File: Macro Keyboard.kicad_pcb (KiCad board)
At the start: 2 copper layers, 101.6 x 123.4 mm, 136 parts, among them J2901 FPC 1x24, Q2901 Q_PJFET_GDS, SW1001 KH-PS1611-54, SW1101 KH-PS1611-54, SW1201 KH-PS1611-54, SW1301 KH-PS1611-54, SW1401 KH-PS1611-54, SW1501 KH-PS1611-54, SW2801 SWITCH TACTILE SPST-NO 50MA 1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, SW601 KH-PS1611-54, SW701 KH-PS1611-54, SW801 KH-PS1611-54, SW901 KH-PS1611-54, U2701 PCA9745BTWJ, U2801 Pico-JER, U301 VEML7700, U401 PI4ULS5V201TAEX

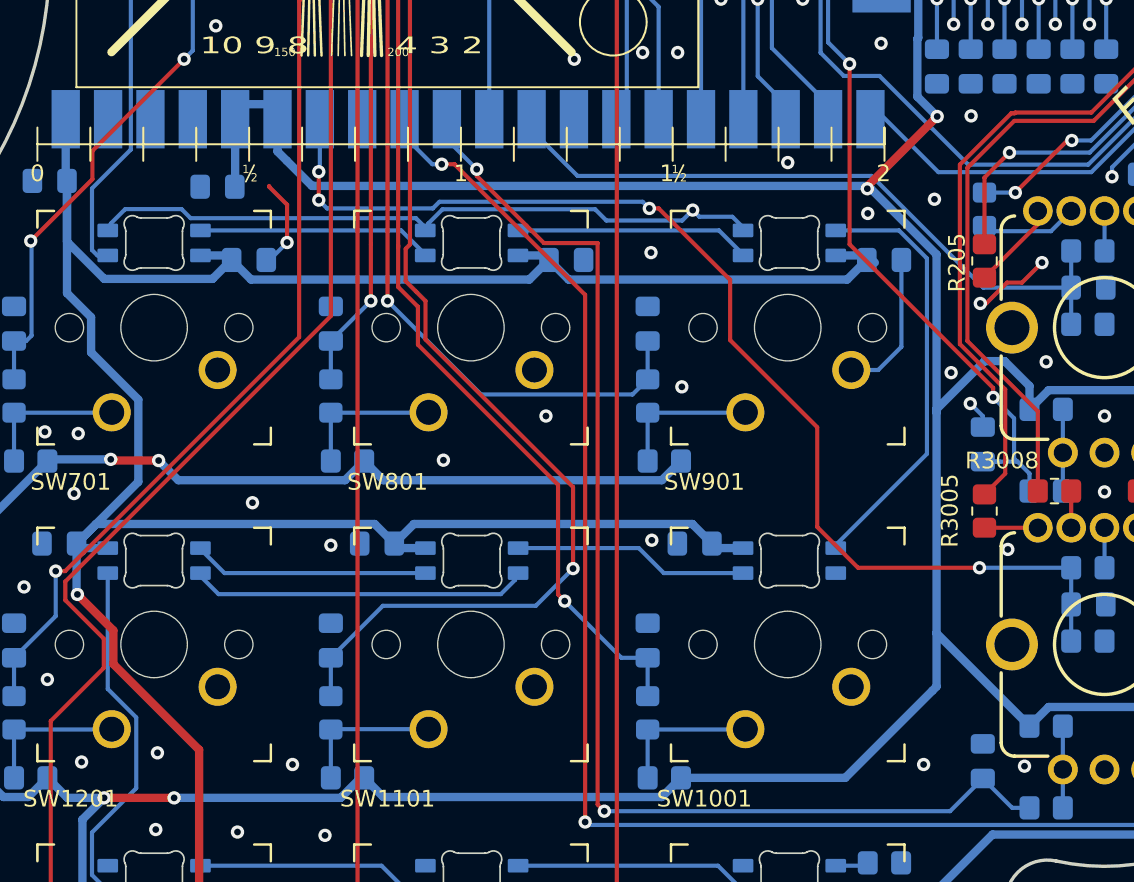
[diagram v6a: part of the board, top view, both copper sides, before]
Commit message: Updated several part orientations to eliminate minimuim clearance issues.
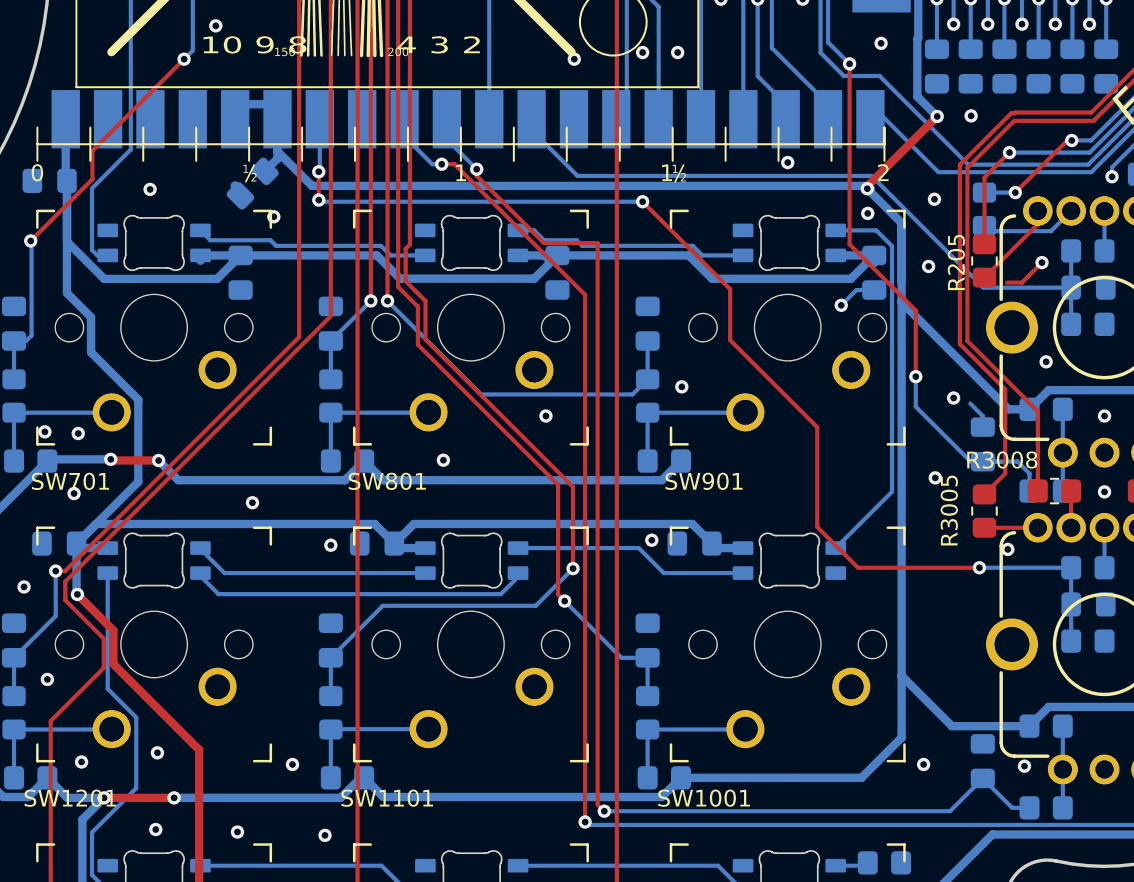
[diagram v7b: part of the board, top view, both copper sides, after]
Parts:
- moved C2801 2.12 mm to (65.9, 81.4), turned to 225 degrees
- moved C2001 0.97 mm to (103.2, 86.7), turned to 90 degrees
- moved C1901 0.93 mm to (84.2, 86.7), turned to 90 degrees
- moved C1801 0.92 mm to (65.2, 86.7), turned to 90 degrees
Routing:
- net GND: track 195.1 -> 139.8 mm
- net /LED 10/Neo LED 05/D_IN: track 26.1 -> 23.3 mm
- net +5V: track 358.7 -> 360.3 mm
- net +3V3: track 463.4 -> 462.3 mm
- net /Pico/GPIO_28_ADC2: track 70.4 -> 69.7 mm

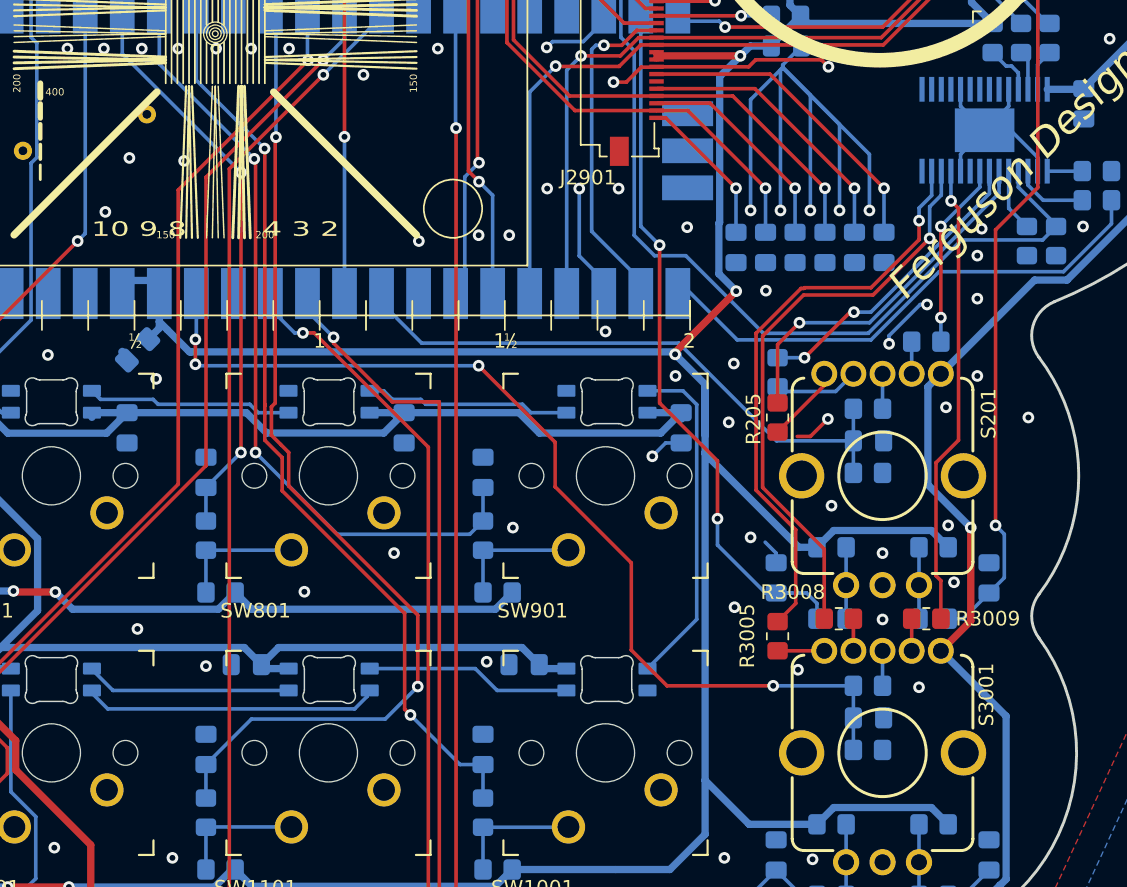
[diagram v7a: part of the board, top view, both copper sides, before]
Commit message: Updated routing to eliminate minimuim clearance issues.
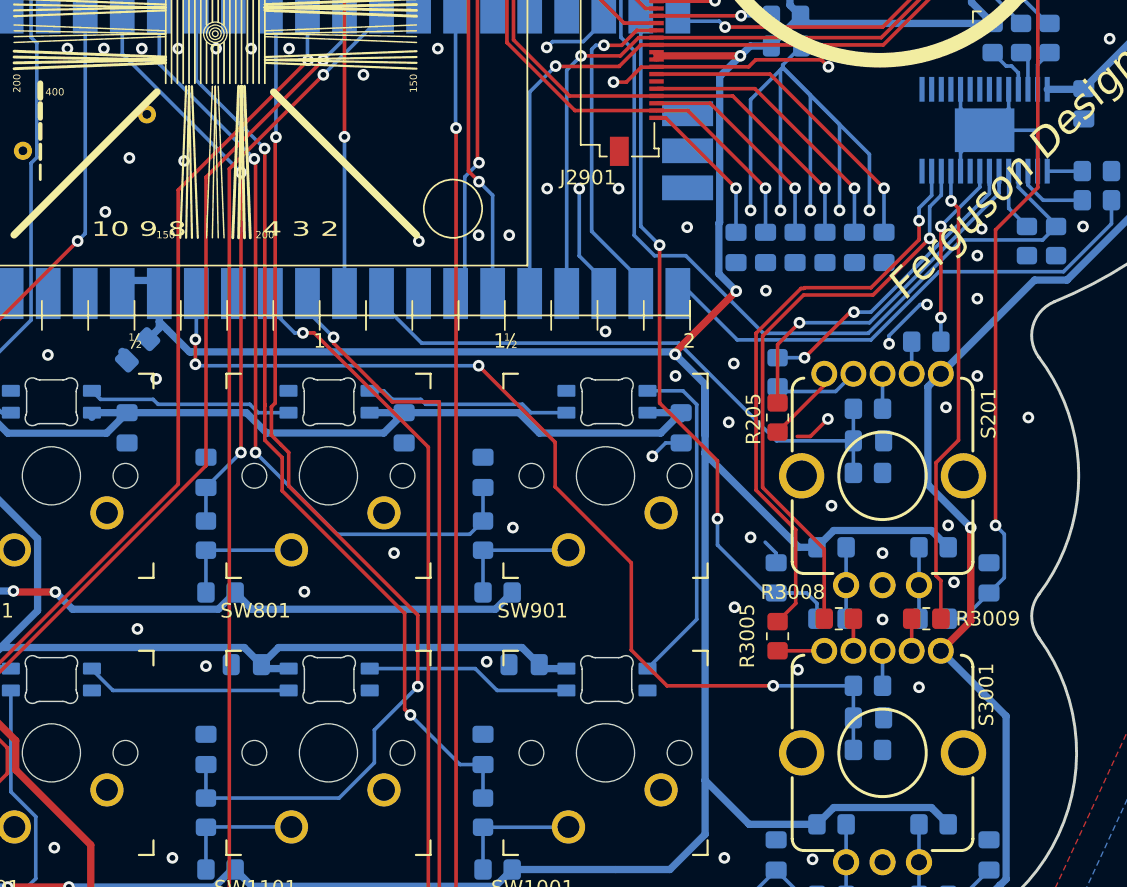
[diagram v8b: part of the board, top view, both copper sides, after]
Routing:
- net GND: track 139.8 -> 122.6 mm
- net /Pico/GPIO_06: track 69.2 -> 71.5 mm
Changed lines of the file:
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@@
     (thickness 1.6)
     (drawings 97)
-    (tracks 1007)
+    (tracks 1008)
     (zones 0)
     (modules 136)
@@
   (via (at 109.9 25.7) (size 0.8) (drill 0.4) (layers F.Cu B.Cu) (net 1))
   (via (at 126.1 25.7) (size 0.8) (drill 0.4) (layers F.Cu B.Cu) (net 1))
-  (segment (start 81.65 105.13) (end 81.65 104.72) (width 0.25) (layer B.Cu) (net 1) (status 20))
-  (segment (start 80.797265 105.982735) (end 81.65 105.13) (width 0.25) (layer B.Cu) (net 1))
-  (segment (start 63.862735 105.982735) (end 80.797265 105.982735) (width 0.25) (layer B.Cu) (net 1))
-  (segment (start 62.6 104.72) (end 63.862735 105.982735) (width 0.25) (layer B.Cu) (net 1) (status 10))
   (via (at 68.7 60.7) (size 0.8) (drill 0.4) (layers F.Cu B.Cu) (net 1))
   (via (at 66.2 60.7) (size 0.8) (drill 0.4) (layers F.Cu B.Cu) (net 1))
@@
   (via (at 114.05 71.8) (size 0.8) (drill 0.4) (layers F.Cu B.Cu) (net 1))
   (via (at 116.1 71.8) (size 0.8) (drill 0.4) (layers F.Cu B.Cu) (net 1))
-  (segment (start 122.349 67.951) (end 124 66.3) (width 0.25) (layer B.Cu) (net 1) (status 20))
-  (segment (start 122.349 69.1067) (end 122.349 67.951) (width 0.25) (layer B.Cu) (net 1) (status 10))
-  (segment (start 125.778802 66.3) (end 124 66.3) (width 0.25) (layer B.Cu) (net 1) (status 30))
-  (segment (start 127.6322 68.153398) (end 125.778802 66.3) (width 0.25) (layer B.Cu) (net 1) (status 20))
-  (segment (start 127.6322 69.1067) (end 127.6322 68.153398) (width 0.25) (layer B.Cu) (net 1) (status 10))
-  (segment (start 122.349 64.649) (end 124 66.3) (width 0.25) (layer B.Cu) (net 1) (status 20))
-  (segment (start 122.349 63.4933) (end 122.349 64.649) (width 0.25) (layer B.Cu) (net 1) (status 10))
-  (segment (start 125.651 64.649) (end 124 66.3) (width 0.25) (layer B.Cu) (net 1) (status 20))
-  (segment (start 125.651 63.4933) (end 125.651 64.649) (width 0.25) (layer B.Cu) (net 1) (status 10))
   (via (at 132.9 49.05) (size 0.8) (drill 0.4) (layers F.Cu B.Cu) (net 1))
   (via (at 129.5 53.45) (size 0.8) (drill 0.4) (layers F.Cu B.Cu) (net 1))
@@
   (segment (start 107.82 61.95) (end 108.3 61.47) (width 0.25) (layer F.Cu) (net 1))
   (segment (start 112.81 61.47) (end 113.29 61.95) (width 0.25) (layer F.Cu) (net 1))
-  (segment (start 108.3 61.47) (end 112.81 61.47) (width 0.25) (layer F.Cu) (net 1))
   (segment (start 109.7 98.0375) (end 110.7375 98.0375) (width 0.25) (layer B.Cu) (net 2) (status 10))
   (segment (start 112.5 98.75) (end 111.775 98.025) (width 0.25) (layer B.Cu) (net 2))
@@
   (via (at 106.45 86.33) (size 0.8) (drill 0.4) (layers F.Cu B.Cu) (net 1))
   (via (at 106.85 99.01) (size 0.8) (drill 0.4) (layers F.Cu B.Cu) (net 1))
+  (segment (start 108.3 61.47) (end 112.81 61.47) (width 0.25) (layer F.Cu) (net 1))
+  (segment (start 125.778802 66.3) (end 124 66.3) (width 0.25) (layer B.Cu) (net 1))
+  (segment (start 127.6322 69.1067) (end 127.6322 66.3122) (width 0.25) (layer B.Cu) (net 1))
+  (segment (start 127.62 66.3) (end 124 66.3) (width 0.25) (layer B.Cu) (net 1))
+  (segment (start 127.6322 66.3122) (end 127.62 66.3) (width 0.25) (layer B.Cu) (net 1))
+  (segment (start 122.349 69.1067) (end 122.349 67.831) (width 0.25) (layer B.Cu) (net 1))
+  (segment (start 123.88 66.3) (end 124 66.3) (width 0.25) (layer B.Cu) (net 1))
+  (segment (start 122.349 67.831) (end 123.88 66.3) (width 0.25) (layer B.Cu) (net 1))
+  (segment (start 122.349 63.4933) (end 122.349 64.799) (width 0.25) (layer B.Cu) (net 1))
+  (segment (start 123.85 66.3) (end 124 66.3) (width 0.25) (layer B.Cu) (net 1))
+  (segment (start 122.349 64.799) (end 123.85 66.3) (width 0.25) (layer B.Cu) (net 1))
+  (segment (start 125.651 63.4933) (end 125.651 64.799) (width 0.25) (layer B.Cu) (net 1))
+  (segment (start 124.15 66.3) (end 124 66.3) (width 0.25) (layer B.Cu) (net 1))
+  (segment (start 125.651 64.799) (end 124.15 66.3) (width 0.25) (layer B.Cu) (net 1))
   (segment (start 108.975 98.0375) (end 105.680911 94.743411) (width 0.25) (layer B.Cu) (net 2))
   (segment (start 109.7 98.0375) (end 108.975 98.0375) (width 0.25) (layer B.Cu) (net 2))
@@
   (segment (start 75.1 58.9) (end 75.02 58.82) (width 0.25) (layer B.Cu) (net 12) (status 30))
   (via (at 85.125 104.45) (size 0.8) (drill 0.4) (layers F.Cu B.Cu) (net 12))
-  (segment (start 82.893901 106.681099) (end 85.125 104.45) (width 0.25) (layer B.Cu) (net 12))
-  (segment (start 73.718901 106.681099) (end 82.893901 106.681099) (width 0.25) (layer B.Cu) (net 12))
-  (segment (start 70.6 109.8) (end 73.718901 106.681099) (width 0.25) (layer B.Cu) (net 12) (status 10))
-  (segment (start 76.275011 90.706985) (end 76.275011 88.400011) (width 0.25) (layer F.Cu) (net 12))
-  (segment (start 85.125 99.556974) (end 76.275011 90.706985) (width 0.25) (layer F.Cu) (net 12))
-  (segment (start 85.125 104.45) (end 85.125 99.556974) (width 0.25) (layer F.Cu) (net 12))
-  (segment (start 76.275011 88.400011) (end 75.725 87.85) (width 0.25) (layer F.Cu) (net 12))
-  (segment (start 75.087664 87.212664) (end 75.087664 85.274054) (width 0.25) (layer F.Cu) (net 12))
-  (via (at 75.400153 66.775153) (size 0.8) (drill 0.4) (layers F.Cu B.Cu) (net 12))
-  (segment (start 75.344762 66.830544) (end 75.400153 66.775153) (width 0.25) (layer F.Cu) (net 12))
-  (segment (start 75.344762 85.016956) (end 75.344762 66.830544) (width 0.25) (layer F.Cu) (net 12))
-  (segment (start 75.087664 85.274054) (end 75.344762 85.016956) (width 0.25) (layer F.Cu) (net 12))
-  (segment (start 75.400153 59.200153) (end 75.02 58.82) (width 0.25) (layer B.Cu) (net 12) (status 30))
-  (segment (start 75.400153 66.775153) (end 75.400153 59.200153) (width 0.25) (layer B.Cu) (net 12) (status 20))
   (segment (start 75.725 87.85) (end 75.087664 87.212664) (width 0.25) (layer F.Cu) (net 12))
+  (segment (start 75.400153 66.775153) (end 75.400153 59.200153) (width 0.25) (layer B.Cu) (net 12) (status 20))
+  (segment (start 75.400153 59.200153) (end 75.02 58.82) (width 0.25) (layer B.Cu) (net 12) (status 30))
+  (segment (start 75.087664 85.274054) (end 75.344762 85.016956) (width 0.25) (layer F.Cu) (net 12))
+  (segment (start 75.344762 85.016956) (end 75.344762 66.830544) (width 0.25) (layer F.Cu) (net 12))
+  (segment (start 75.344762 66.830544) (end 75.400153 66.775153) (width 0.25) (layer F.Cu) (net 12))
+  (via (at 75.400153 66.775153) (size 0.8) (drill 0.4) (layers F.Cu B.Cu) (net 12))
+  (segment (start 75.087664 87.212664) (end 75.087664 85.274054) (width 0.25) (layer F.Cu) (net 12))
+  (segment (start 76.275011 88.400011) (end 75.725 87.85) (width 0.25) (layer F.Cu) (net 12))
+  (segment (start 85.125 104.45) (end 85.125 99.556974) (width 0.25) (layer F.Cu) (net 12))
+  (segment (start 85.125 99.556974) (end 76.275011 90.706985) (width 0.25) (layer F.Cu) (net 12))
+  (segment (start 76.275011 90.706985) (end 76.275011 88.400011) (width 0.25) (layer F.Cu) (net 12))
+  (segment (start 82.15 109.68) (end 82.15 107.425) (width 0.25) (layer B.Cu) (net 12))
+  (segment (start 82.15 107.425) (end 85.125 104.45) (width 0.25) (layer B.Cu) (net 12))
+  (segment (start 79.73 112.1) (end 82.15 109.68) (width 0.25) (layer B.Cu) (net 12))
+  (segment (start 70.6 112.1) (end 79.73 112.1) (width 0.25) (layer B.Cu) (net 12))
   (segment (start 51.6 112.1) (end 51.6 109.8) (width 0.25) (layer B.Cu) (net 13) (status 30))
   (via (at 54.1 104.6) (size 0.8) (drill 0.4) (layers F.Cu B.Cu) (net 13))
